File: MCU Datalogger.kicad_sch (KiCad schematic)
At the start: 25 parts, among them U1 DS1337S_, U2 24LC1025, U3 24LC1025, U4 ATMEGA328P-AU, Y1 32.768 KHz, Y2 16 MHz

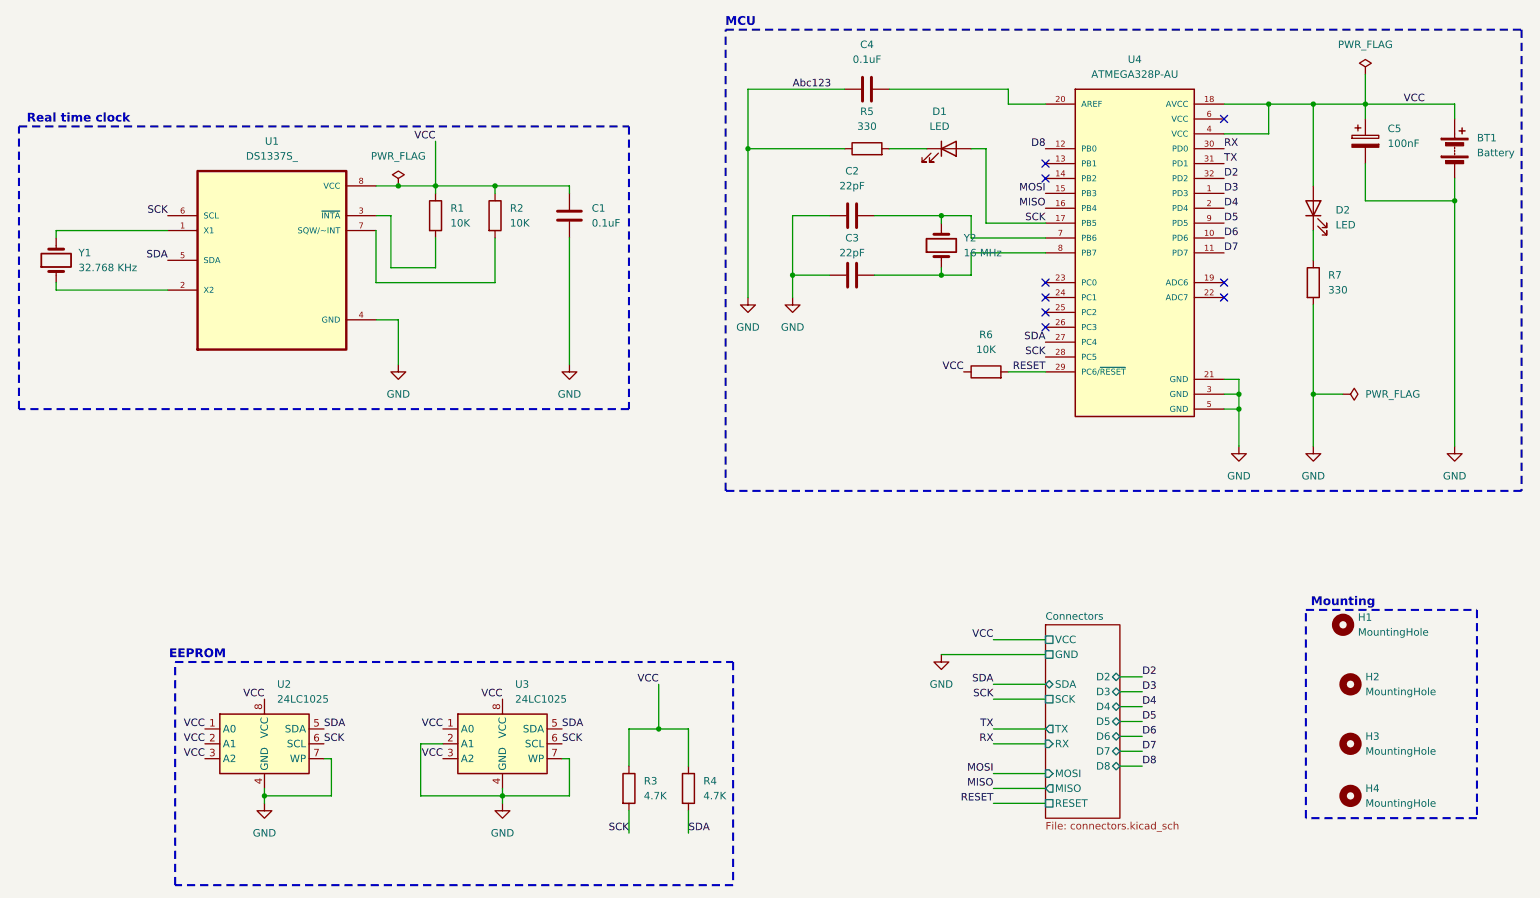
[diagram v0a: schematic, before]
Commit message: fix wrong SCL/SCK connection
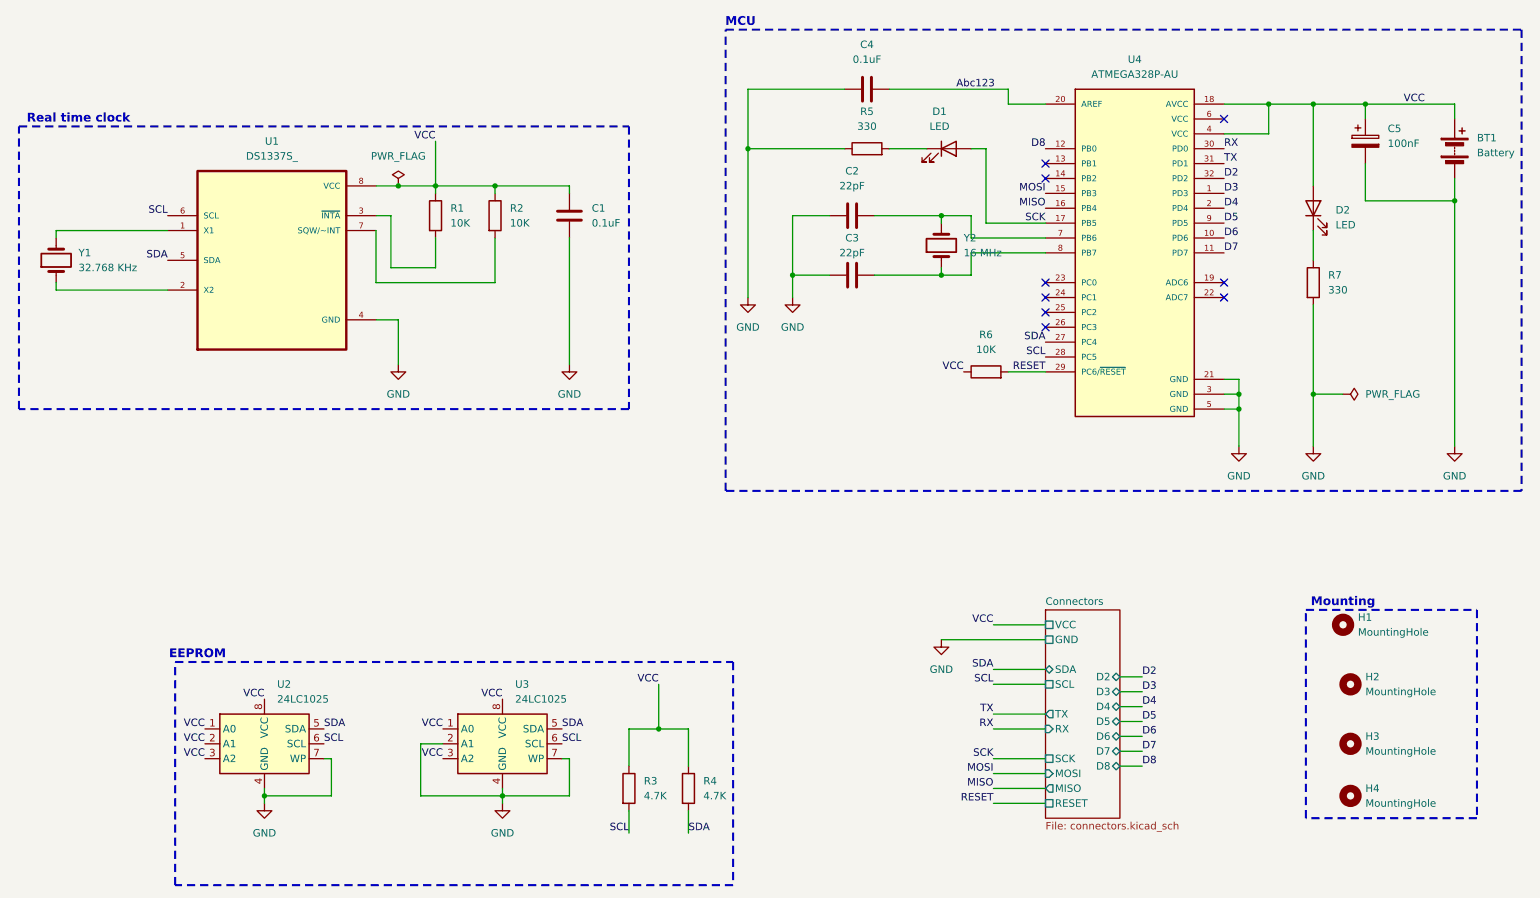
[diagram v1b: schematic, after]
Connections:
- net SCK: no longer R3.2, U1.6 (SCL), U2.6 (SCL), U3.6 (SCL), U4.28 (PC5)
- net Abc123: now reaches C4.2, U4.20 (AREF)
- new net SCL: R3.2, U1.6 (SCL), U2.6 (SCL), U3.6 (SCL), U4.28 (PC5)
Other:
- sheet Connectors ports: added SCL; removed none
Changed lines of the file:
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@@
 	(wire
 		(pts
-			(xy 190.5 138.43) (xy 199.39 138.43)
+			(xy 190.5 135.89) (xy 199.39 135.89)
 		)
 		(stroke
@@
 	(wire
 		(pts
-			(xy 190.5 123.19) (xy 199.39 123.19)
+			(xy 190.5 120.65) (xy 199.39 120.65)
 		)
 		(stroke
@@
 	(wire
 		(pts
-			(xy 190.5 133.35) (xy 199.39 133.35)
+			(xy 190.5 130.81) (xy 199.39 130.81)
 		)
 		(stroke
@@
 	(wire
 		(pts
+			(xy 190.5 143.51) (xy 199.39 143.51)
+		)
+		(stroke
+			(width 0)
+			(type default)
+		)
+	)
+	(wire
+		(pts
 			(xy 181.61 50.8) (xy 181.61 52.07)
 		)
@@
 	(wire
 		(pts
-			(xy 190.5 140.97) (xy 199.39 140.97)
+			(xy 190.5 138.43) (xy 199.39 138.43)
 		)
 		(stroke
@@
 	(wire
 		(pts
-			(xy 254 26.67) (xy 254 31.75)
-		)
-		(stroke
-			(width 0)
-			(type default)
-		)
-	)
-	(wire
-		(pts
 			(xy 92.71 149.86) (xy 106.68 149.86)
 		)
@@
 	(wire
 		(pts
-			(xy 190.5 130.81) (xy 199.39 130.81)
+			(xy 190.5 128.27) (xy 199.39 128.27)
 		)
 		(stroke
@@
 	(wire
 		(pts
-			(xy 181.61 125.73) (xy 199.39 125.73)
-		)
-		(stroke
-			(width 0)
-			(type default)
-		)
-	)
-	(wire
-		(pts
 			(xy 170.18 60.96) (xy 181.61 60.96)
 		)
@@
 	(wire
 		(pts
+			(xy 181.61 123.19) (xy 199.39 123.19)
+		)
+		(stroke
+			(width 0)
+			(type default)
+		)
+	)
+	(wire
+		(pts
 			(xy 156.21 50.8) (xy 156.21 60.96)
 		)
@@
 		)
 	)
+	(label "SCK"
+		(at 190.5 143.51 180)
+		(effects
+			(font
+				(size 1.27 1.27)
+			)
+			(justify right bottom)
+		)
+	)
 	(label "VCC"
 		(at 185.42 77.47 180)
@@
 		)
 	)
-	(label "SCK"
+	(label "SCL"
 		(at 76.2 140.97 0)
 		(effects
@@
 		)
 	)
-	(label "SCK"
+	(label "SCL"
 		(at 49.53 50.8 180)
 		(effects
@@
 	)
 	(label "TX"
-		(at 190.5 138.43 180)
+		(at 190.5 135.89 180)
 		(effects
 			(font
@@
 		)
 	)
-	(label "SCK"
+	(label "SCL"
 		(at 116.84 140.97 0)
 		(effects
@@
 	)
 	(label "RX"
-		(at 190.5 140.97 180)
+		(at 190.5 138.43 180)
 		(effects
 			(font
@@
 		)
 	)
-	(label "SCK"
-		(at 190.5 133.35 180)
+	(label "SCL"
+		(at 190.5 130.81 180)
 		(effects
 			(font
@@
 		)
 	)
-	(label "SCK"
+	(label "SCL"
 		(at 128.27 156.21 180)
 		(effects
@@
 	)
 	(label "VCC"
-		(at 190.5 123.19 180)
+		(at 190.5 120.65 180)
 		(effects
 			(font
@@
 		)
 	)
-	(label "SCK"
+	(label "SCL"
 		(at 199.39 74.93 180)
 		(effects
@@
 		)
 	)
-	(label "Abc123"
-		(at 156.21 29.21 0)
+	(label "D7"
+		(at 215.9 142.24 0)
 		(effects
 			(font
@@
 		)
 	)
-	(label "D7"
-		(at 215.9 142.24 0)
+	(label "RESET"
+		(at 190.5 151.13 180)
 		(effects
 			(font
 				(size 1.27 1.27)
 			)
-			(justify left bottom)
+			(justify right bottom)
 		)
 	)
-	(label "RESET"
-		(at 190.5 151.13 180)
+	(label "Abc123"
+		(at 184.15 29.21 0)
 		(effects
 			(font
 				(size 1.27 1.27)
 			)
-			(justify right bottom)
+			(justify left bottom)
 		)
 	)
@@
 	)
 	(label "SDA"
-		(at 190.5 130.81 180)
+		(at 190.5 128.27 180)
 		(effects
 			(font
@@
 	)
 	(symbol
-		(lib_id "power:PWR_FLAG")
-		(at 254 26.67 0)
-		(unit 1)
-		(exclude_from_sim no)
-		(in_bom yes)
-		(on_board yes)
-		(dnp no)
-		(fields_autoplaced yes)
-		(property "Reference" "#FLG02"
-			(at 254 24.765 0)
-			(effects
-				(font
-					(size 1.27 1.27)
-				)
-				(hide yes)
-			)
-		)
-		(property "Value" "PWR_FLAG"
-			(at 254 21.59 0)
-			(effects
-				(font
-					(size 1.27 1.27)
-				)
-			)
-		)
-		(property "Footprint" ""
-			(at 254 26.67 0)
-			(effects
-				(font
-					(size 1.27 1.27)
-				)
-				(hide yes)
-			)
-		)
-		(property "Datasheet" "~"
-			(at 254 26.67 0)
-			(effects
-				(font
-					(size 1.27 1.27)
-				)
-				(hide yes)
-			)
-		)
-		(property "Description" "Special symbol for telling ERC where power comes from"
-			(at 254 26.67 0)
-			(effects
-				(font
-					(size 1.27 1.27)
-				)
-				(hide yes)
-			)
-		)
-		(pin "1"
-		)
-		(instances
-			(project ""
-				(path "/c1519fa5-dbfa-43a9-bb02-bb0bfad7a63d"
-					(reference "#FLG02")
-					(unit 1)
-				)
-			)
-		)
-	)
-	(symbol
 		(lib_id "Device:R")
 		(at 189.23 77.47 90)
@@
 	(symbol
 		(lib_id "power:GND")
-		(at 181.61 125.73 0)
+		(at 181.61 123.19 0)
 		(unit 1)
 		(exclude_from_sim no)
@@
 		(fields_autoplaced yes)
 		(property "Reference" "#PWR07"
-			(at 181.61 132.08 0)
+			(at 181.61 129.54 0)
 			(effects
 				(font
@@
 		)
 		(property "Value" "GND"
-			(at 181.61 130.81 0)
+			(at 181.61 128.27 0)
 			(effects
 				(font
@@
 		)
 		(property "Footprint" ""
-			(at 181.61 125.73 0)
+			(at 181.61 123.19 0)
 			(effects
 				(font
@@
 		)
 		(property "Datasheet" ""
-			(at 181.61 125.73 0)
+			(at 181.61 123.19 0)
 			(effects
 				(font
@@
 		)
 		(property "Description" "Power symbol creates a global label with name \"GND\" , ground"
-			(at 181.61 125.73 0)
+			(at 181.61 123.19 0)
 			(effects
 				(font
@@
 	)
 	(sheet
-		(at 199.39 120.65)
-		(size 12.7 33.02)
+		(at 199.39 118.11)
+		(size 12.7 35.56)
 		(exclude_from_sim no)
 		(in_bom yes)
@@
 		)
 		(property "Sheetname" "Connectors"
-			(at 199.39 119.9384 0)
+			(at 199.39 117.3984 0)
 			(effects
 				(font
@@
 		)
 		(pin "TX" output
-			(at 199.39 138.43 180)
+			(at 199.39 135.89 180)
 			(effects
 				(font
@@
 			)
 		)
-		(pin "SCK" passive
-			(at 199.39 133.35 180)
+		(pin "SCL" passive
+			(at 199.39 130.81 180)
 			(effects
 				(font
@@
 		)
 		(pin "VCC" passive
-			(at 199.39 123.19 180)
+			(at 199.39 120.65 180)
 			(effects
 				(font
@@
 		)
 		(pin "SDA" bidirectional
-			(at 199.39 130.81 180)
+			(at 199.39 128.27 180)
 			(effects
 				(font
@@
 		)
 		(pin "GND" passive
-			(at 199.39 125.73 180)
+			(at 199.39 123.19 180)
 			(effects
 				(font
@@
 		)
 		(pin "RX" input
-			(at 199.39 140.97 180)
+			(at 199.39 138.43 180)
 			(effects
 				(font
@@
 			(effects
 				(font
+					(size 1.27 1.27)
+				)
+				(justify left)
+			)
+		)
+		(pin "SCK" passive
+			(at 199.39 143.51 180)
+			(effects
+				(font
